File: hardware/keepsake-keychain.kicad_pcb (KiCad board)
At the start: 2 copper layers, 80 x 30 mm, 94 parts, among them Q1 MMFTP4042K, Q2 MMFTP4042K, Q3 MMFTP4042K, Q4 MMFTP4042K, SW1 SPDT Power Switch, SW2 PTS636 SK25J SMTR LFS, U1 74HC595 BLUE Shift Register, U2 74HC595 GREEN Shift Register, U3 74HC595 RED Shift Register, U4 ATTINY1614, U5 Op Amp, U6 MEMS Microphone

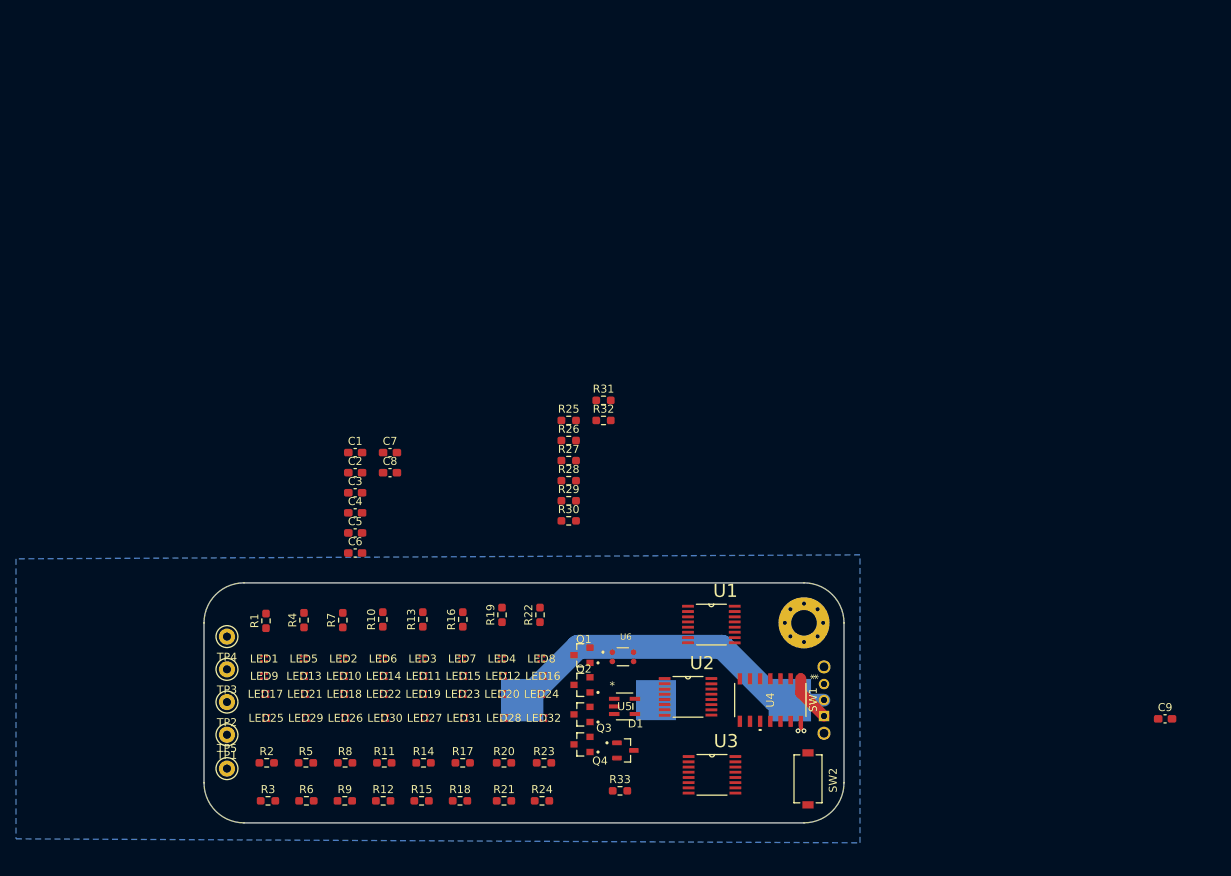
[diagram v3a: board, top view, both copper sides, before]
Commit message: Rename nets, move resistors to rear
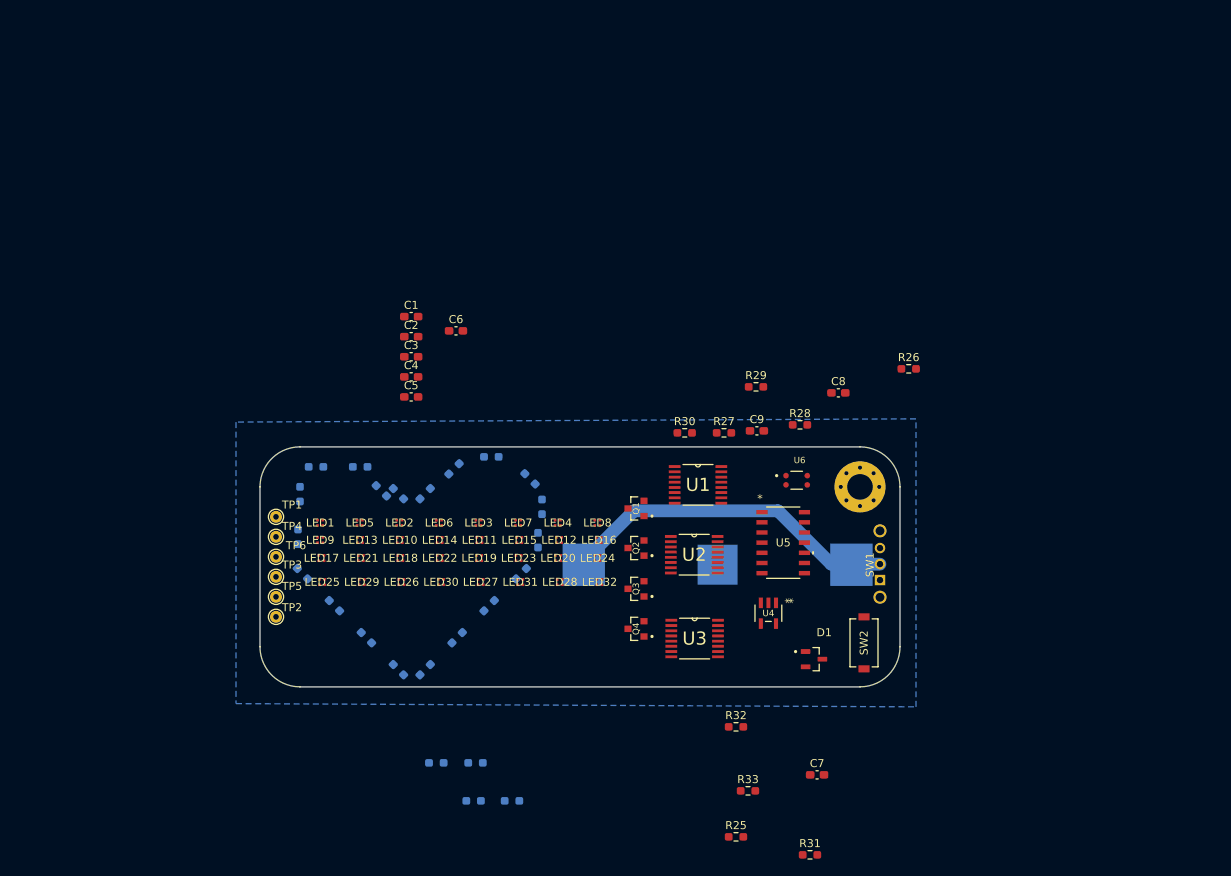
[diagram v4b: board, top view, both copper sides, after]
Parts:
- added TP6: 5002, TestPoint:TestPoint_THTPad_D1.5mm_Drill0.7mm, F.Cu at (112.5, 99.8)
- R1, R10, R11, R12, R13, R14, R15, R16, R17, R18, R19, R2, R20, R21, R22, R23, R24, R3, R4, R5, R6, R7, R8, R9: moved to B.Cu
- TP1, TP2, TP3, TP4, TP5: footprint digikey-footprints:Test_Point_D1.02mm -> TestPoint:TestPoint_THTPad_D1.5mm_Drill0.7mm
- U1: value 74HC595 BLUE Shift Register -> 74HC595
- U2: value 74HC595 GREEN Shift Register -> 74HC595
- U3: value 74HC595 RED Shift Register -> 74HC595
- U4: value ATTINY1614 -> Op Amp; footprint 0_ATtiny1614:SOIC14_SL_MCH -> 0_Op_Amp:SOT-23-5_MC_MCH
- U5: value Op Amp -> ATTINY1614; footprint 0_Op_Amp:SOT-23-5_MC_MCH -> 0_ATtiny1614:SOIC14_SL_MCH
- moved C7 66.9 mm to (180.1, 127.0)
- moved C9 62.4 mm to (172.6, 84.0)
- moved R31 62.4 mm to (179.2, 137.0)
- moved C8 56.9 mm to (182.8, 79.2)
- moved R25 56.1 mm to (170.0, 134.8)
- moved R26 43.4 mm to (191.6, 76.2)
- moved R32 41.7 mm to (170.0, 121.0)
- moved R6 40.1 mm to (127.8, 91.9), turned to 135 degrees
- moved R9 39.7 mm to (131.1, 91.9), turned to 45 degrees
- moved R12 38.8 mm to (125.7, 91.5), turned to 135 degrees
- moved R8 37.0 mm to (123.0, 88.5), turned to 180 degrees
- moved U6 31.0 mm to (177.6, 90.2)
- moved C6 30.5 mm to (135.0, 71.5)
- moved R28 29.7 mm to (178.0, 83.2)
- moved R3 28.7 mm to (115.8, 101.9), turned to 135 degrees
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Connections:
- C8 pad 2: Net-(U5-VIN+) -> Net-(U4-VIN+)
- D1 pad 1: Net-(U5-VOUT) -> Net-(U4-VOUT)
- R25 pad 1: Net-(U5-VOUT) -> Net-(U4-VOUT)
- R25 pad 2: Net-(U5-VIN-) -> Net-(U4-VIN-)
- R26 pad 1: Net-(U4-PA0/*RESET/UPDI) -> Net-(U5-PA0/*RESET/UPDI)
- R28 pad 1: Net-(U5-VIN-) -> Net-(U4-VIN-)
- SW2 pad 1: Net-(U4-PB0) -> Net-(U5-PB0)
- TP1 pad 1: GND -> +3V3
- TP2 pad 1: Net-(U4-PA0/*RESET/UPDI) -> GND
- TP3 pad 1: MIC -> Net-(U5-PA0/*RESET/UPDI)
- TP4 pad 1: Net-(U4-TOSC1/PB3) -> MIC
- TP5 pad 1: Net-(U4-TOSC2/PB2) -> Net-(U5-TOSC1/PB3)
- U4 pad 1: +3V3 -> Net-(U4-VOUT)
- U4 pad 2: S_ROW_0 -> GND
- U4 pad 3: S_ROW_1 -> Net-(U4-VIN+)
- U4 pad 4: S_ROW_2 -> Net-(U4-VIN-)
- U4 pad 5: S_ROW_3 -> +3V3
- U5 pad 1: Net-(U5-VOUT) -> +3V3
- U5 pad 2: GND -> S_ROW_0
- U5 pad 3: Net-(U5-VIN+) -> S_ROW_1
- U5 pad 4: Net-(U5-VIN-) -> S_ROW_2
- U5 pad 5: +3V3 -> S_ROW_3
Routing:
- net +3V3: track 5.85 -> 0.00 mm
- net GND: track 2.69 -> 0.00 mm, vias 2 -> 0

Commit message: Finish heart, refine references designator positions
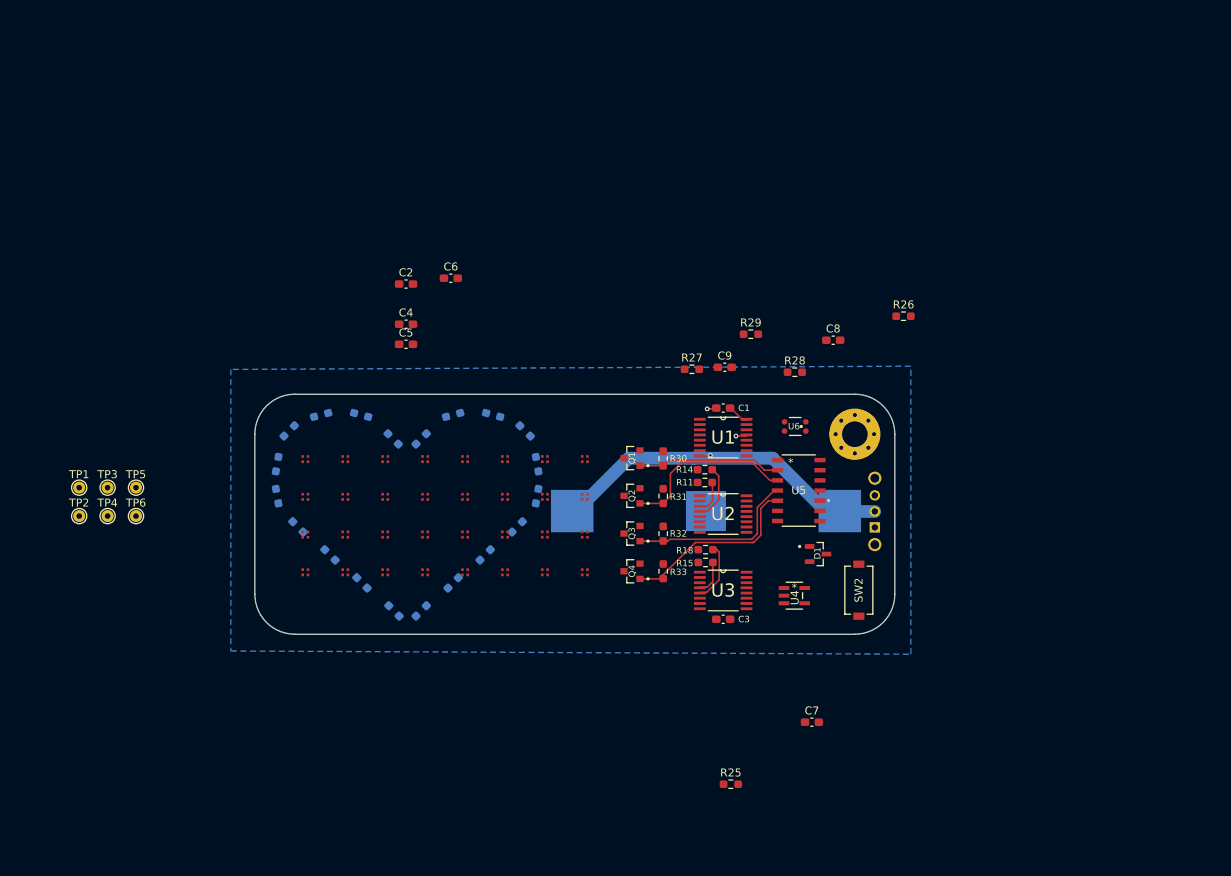
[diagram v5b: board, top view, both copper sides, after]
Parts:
- R11, R14, R15, R18: moved to F.Cu
- moved C3 51.0 mm to (168.4, 107.6), turned to 180 degrees
- moved R11 48.5 mm to (166.1, 90.5), turned to 0 degrees
- moved R31 48.5 mm to (160.9, 92.2), turned to 90 degrees
- moved R14 46.5 mm to (166.1, 88.9), turned to 0 degrees
- moved R15 41.6 mm to (166.2, 100.5), turned to 0 degrees
- moved C1 40.6 mm to (168.4, 81.2), turned to 180 degrees
- moved R18 39.6 mm to (166.2, 98.9), turned to 0 degrees
- moved R33 29.4 mm to (160.9, 101.6), turned to 90 degrees
- moved TP2 27.6 mm to (87.9, 94.7), turned to 0 degrees
- moved R32 25.8 mm to (160.9, 96.9), turned to 90 degrees
- moved TP1 24.9 mm to (87.9, 91.1), turned to 0 degrees
- moved TP3 23.8 mm to (91.5, 91.1), turned to 0 degrees
- moved TP5 22.2 mm to (95.0, 91.1)
- moved TP4 21.2 mm to (91.5, 94.7), turned to 0 degrees
- moved TP6 18.2 mm to (95.0, 94.7)
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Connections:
- BT1 pad 1: Net-(BT1-Pad1) -> GND
- SW1 pad 2: Net-(BT1-Pad1) -> GND
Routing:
- net GND: track 0.00 -> 47.2 mm, vias 0 -> 3
- net Net-(BT1-Pad1): track 43.3 -> 0.00 mm
- net S_ROW_3: track 0.00 -> 23.5 mm
- net S_ROW_1: track 0.00 -> 21.8 mm
- net S_ROW_2: track 0.00 -> 21.7 mm
- net S_ROW_0: track 0.00 -> 18.0 mm
- net Net-(U3-Q5): track 0.00 -> 7.45 mm
- net Net-(U2-Q4): track 0.00 -> 7.07 mm
- net Net-(U3-Q4): track 0.00 -> 4.30 mm
- net Net-(U2-Q3): track 0.00 -> 3.98 mm
- net +3V3: track 0.00 -> 2.44 mm

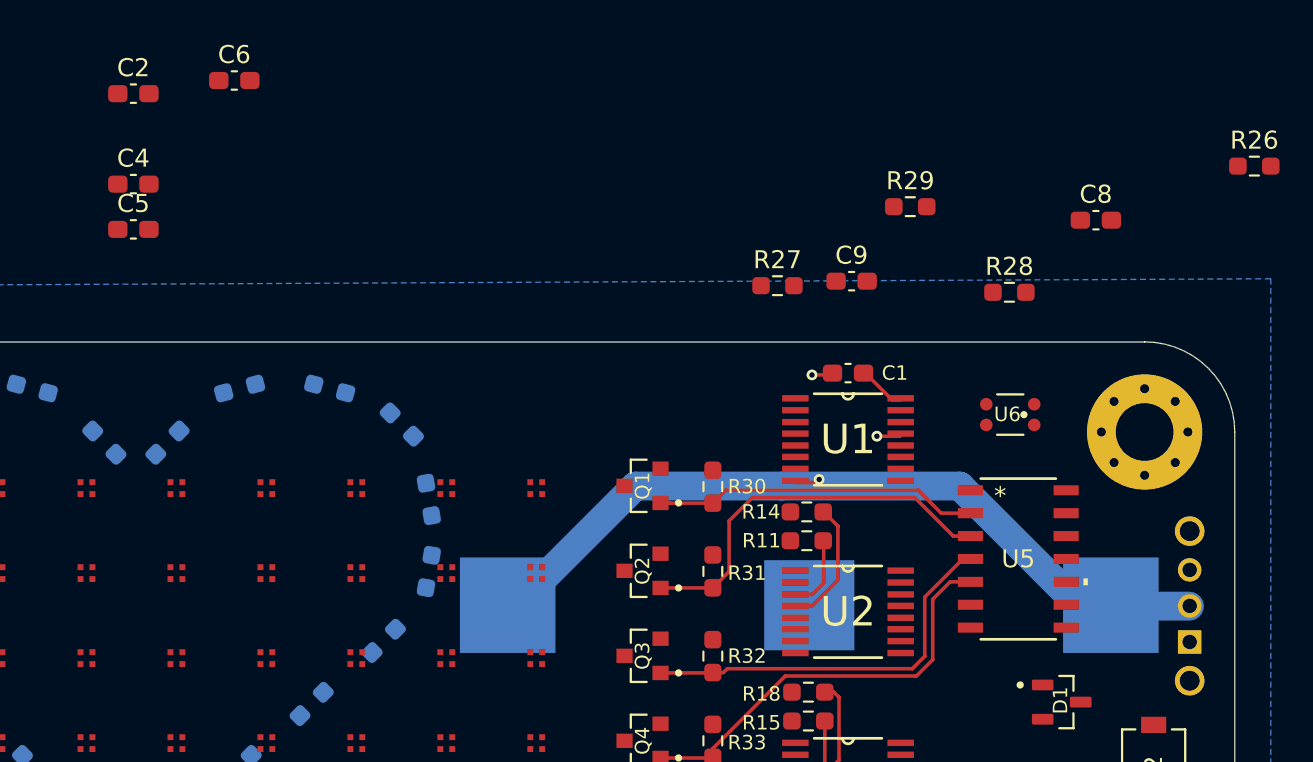
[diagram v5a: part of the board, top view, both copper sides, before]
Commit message: Fix broken net, fix via annular ring constraint
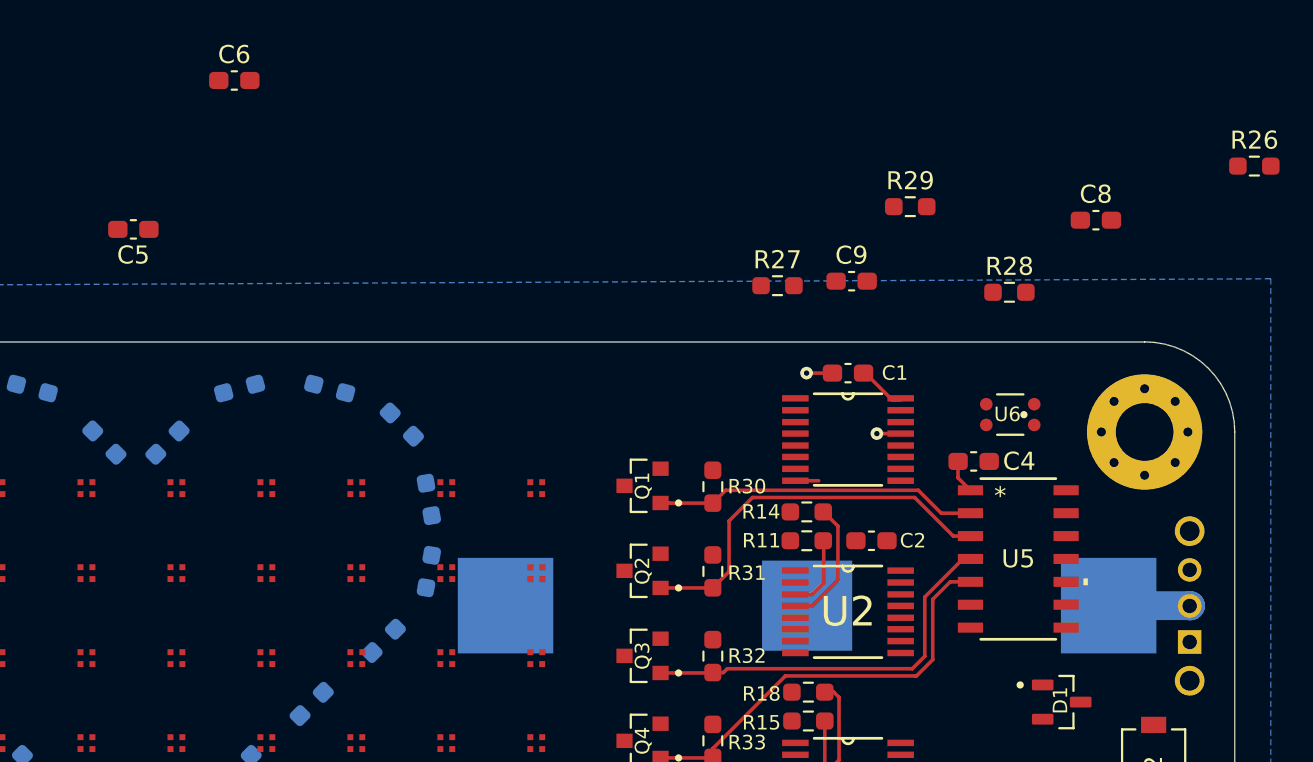
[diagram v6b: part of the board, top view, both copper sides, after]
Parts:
- moved C4 49.1 mm to (175.4, 86.1)
- moved C2 47.9 mm to (169.7, 90.5), turned to 180 degrees
- moved BT1 0.12 mm to (166.1, 94.1)
- turned C5 to 180 degrees
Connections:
- BT1 pad 1: GND -> Net-(BT1-Pad1)
- SW1 pad 2: GND -> Net-(BT1-Pad1)
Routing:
- net GND: track 47.2 -> 4.18 mm, vias 3 -> 2
- net Net-(BT1-Pad1): track 0.00 -> 4.59 mm
- net +3V3: track 2.44 -> 4.33 mm

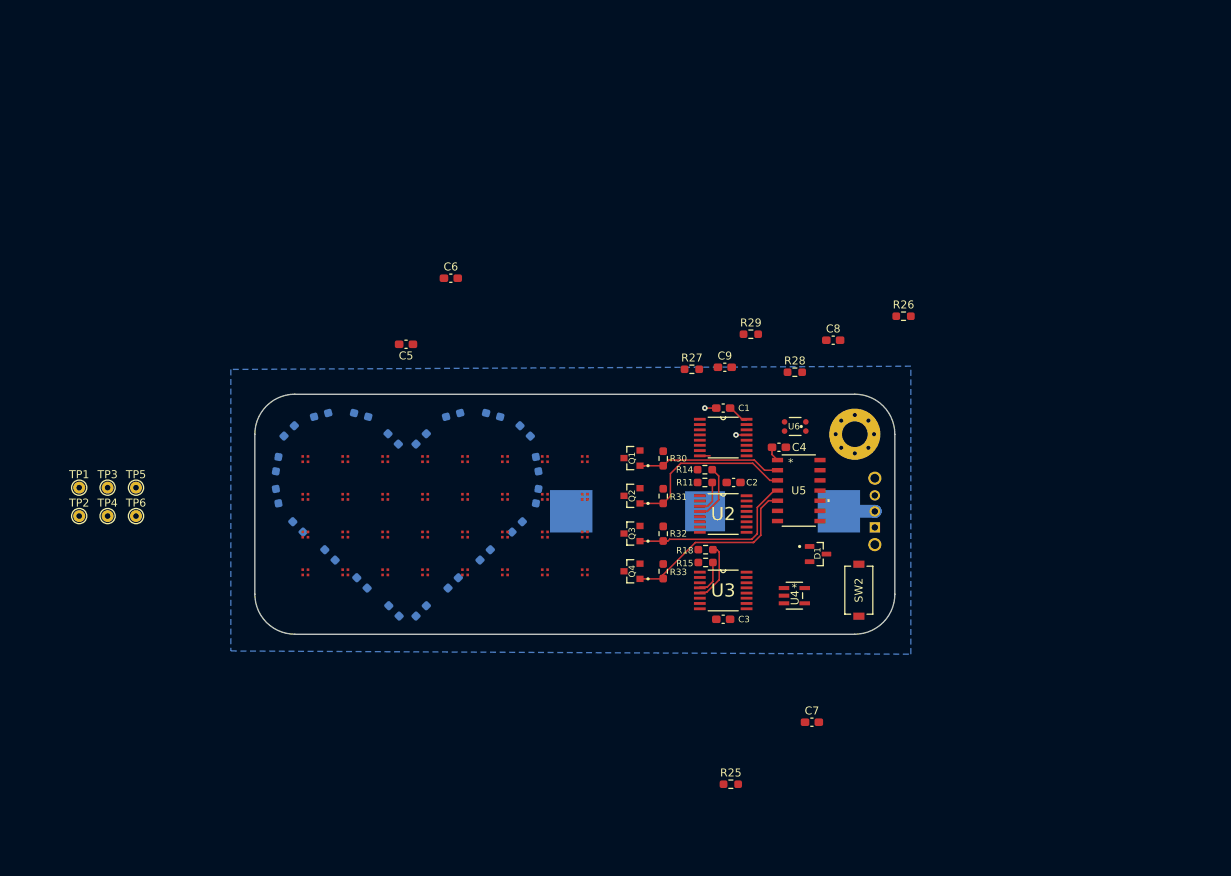
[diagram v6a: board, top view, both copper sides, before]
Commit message: Place remaining passives
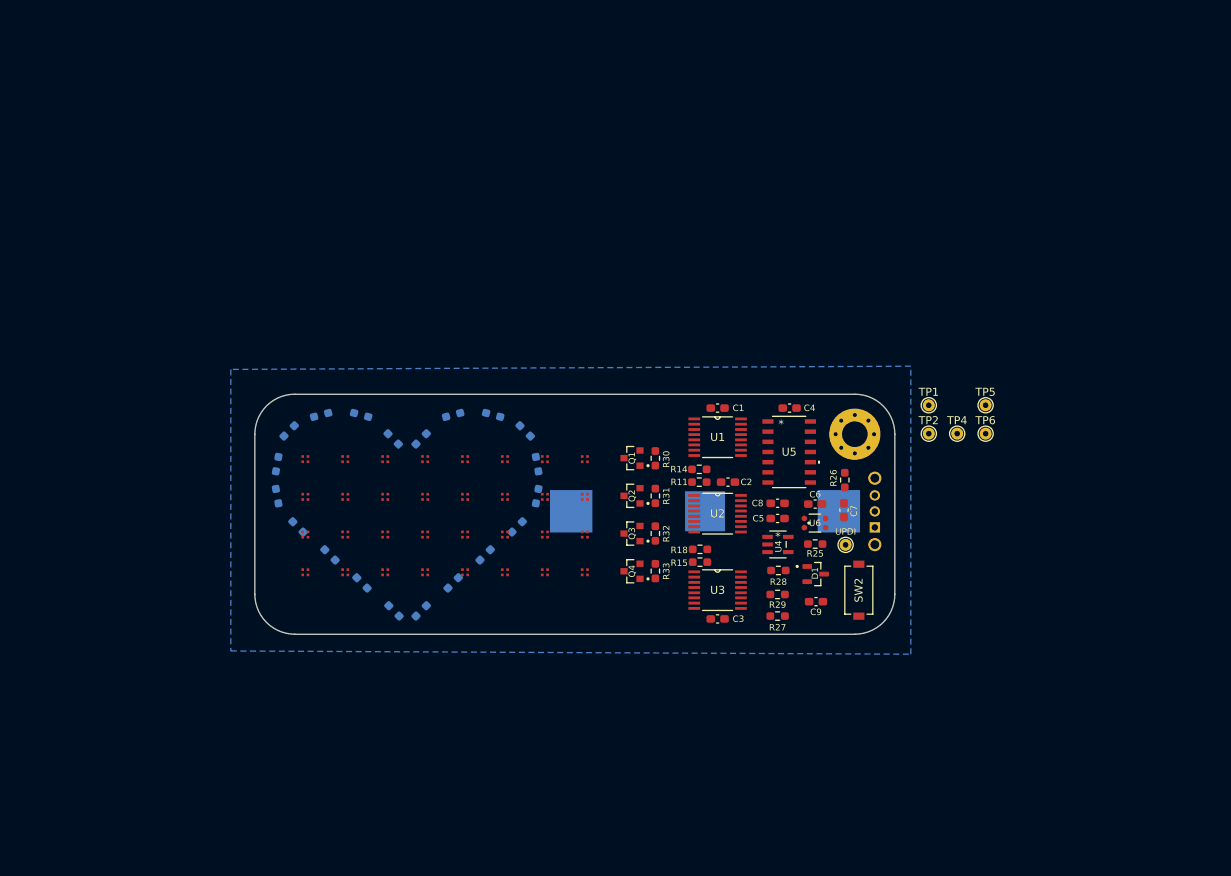
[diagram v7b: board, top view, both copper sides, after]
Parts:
- moved TP4 106.7 mm to (197.7, 84.4)
- moved TP1 106.7 mm to (194.1, 80.8)
- moved TP2 106.7 mm to (194.1, 84.4)
- moved TP5 106.7 mm to (201.2, 80.8)
- moved TP6 106.7 mm to (201.2, 84.4)
- moved UPDI 92.5 mm to (183.7, 98.3)
- moved C6 53.6 mm to (179.9, 93.2)
- moved C5 51.3 mm to (175.2, 95.0), turned to 0 degrees
- moved R29 32.7 mm to (175.2, 104.5)
- moved R27 32.7 mm to (175.2, 107.2), turned to 180 degrees
- moved R25 31.8 mm to (179.9, 98.2)
- moved C9 31.4 mm to (180.0, 105.4)
- moved C7 26.8 mm to (183.5, 93.9), turned to -90 degrees
- moved R28 24.9 mm to (175.3, 101.5), turned to 180 degrees
- moved R26 21.8 mm to (183.6, 90.2), turned to -90 degrees
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- renumbered TP3 to UPDI
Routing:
- net S_ROW_3: track 23.5 -> 0.00 mm
- net S_ROW_1: track 21.8 -> 0.00 mm
- net S_ROW_2: track 21.7 -> 0.00 mm
- net S_ROW_0: track 18.0 -> 0.00 mm
- net Net-(U3-Q5): track 7.45 -> 0.00 mm
- net Net-(U2-Q4): track 7.07 -> 0.00 mm
- net Net-(BT1-Pad1): track 4.59 -> 0.00 mm
- net +3V3: track 4.33 -> 0.00 mm
- net Net-(U3-Q4): track 4.30 -> 0.00 mm
- net GND: track 4.18 -> 0.00 mm, vias 2 -> 0
- net Net-(U2-Q3): track 3.98 -> 0.00 mm
